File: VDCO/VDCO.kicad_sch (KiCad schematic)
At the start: 65 parts, among them J1 Conn_02x05_Counter_Clockwise, J2 ModeCV, J3 Parameter 1 CV, J4 Parameter 2 CV, J5 Gain CV, J6 Output, J7 V/OCT, SW1 Mode Switch On-Off-On, U1 TL072

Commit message: couple changes
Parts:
- C1, C10, C11, C12, C13, C14, C15, C2, C3, C4, C5, C6, C7, C8, C9: footprint Capacitor_THT:C_Disc_D5.0mm_W2.5mm_P5.00mm -> Capacitor_SMD:C_0805_2012Metric_Pad1.18x1.45mm_HandSolder
- D1, D10, D11, D12, D13, D3, D5, D6, D8, D9: footprint Diode_THT:D_DO-35_SOD27_P7.62mm_Horizontal -> Diode_SMD:D_0805_2012Metric_Pad1.15x1.40mm_HandSolder
- D2, D4, D7: footprint LED_THT:LED_D5.0mm -> LED_SMD:LED_0805_2012Metric_Pad1.15x1.40mm_HandSolder
- R1, R10, R11, R12, R13, R14, R15, R16, R17, R18, R19, R2, R20, R21, R22, R23, R3, R4, R5, R6, R7, R8, R9: footprint Resistor_THT:R_Axial_DIN0207_L6.3mm_D2.5mm_P10.16mm_Horizontal -> Resistor_SMD:R_0805_2012Metric_Pad1.20x1.40mm_HandSolder

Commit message: first complete routing of smd board
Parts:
- removed D1, D10, D11, D12, D13, D3, D5, D6, D8, D9: D_Schottky_Small, Diode_SMD:D_0805_2012Metric_Pad1.15x1.40mm_HandSolder, symbol Device:D_Schottky_Small
- removed SW1: Mode Switch On-Off-On, Button_Switch_THT:SW_CuK_JS202011CQN_DPDT_Straight, symbol Switch:SW_SPDT_MSM
- added D2, D4, D6, D7, D8: D_Zener_Small, Diode_SMD:D_0805_2012Metric_Pad1.15x1.40mm_HandSolder, symbol Device:D_Zener_Small
- added SW1: SW_SPDT, Button_Switch_THT:SW_PUSH_6mm_H5mm, symbol Switch:SW_SPST
- C13: renamed from C12; value 4.7u -> 10u
- D1: renamed from D2; footprint LED_SMD:LED_0805_2012Metric_Pad1.15x1.40mm_HandSolder -> LED_THT:LED_D5.0mm
- D3: renamed from D4; footprint LED_SMD:LED_0805_2012Metric_Pad1.15x1.40mm_HandSolder -> LED_THT:LED_D5.0mm
- D5: renamed from D7; footprint LED_SMD:LED_0805_2012Metric_Pad1.15x1.40mm_HandSolder -> LED_THT:LED_D5.0mm
- R14, R16: value 50K -> 47K
- R20: renamed from R18; value 220R -> 1K
- renumbered C13 to C12, J7 to J6, J6 to J7, R21 to R17, R22 to R18, R17 to R19, R19 to R21, R20 to R22
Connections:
- net GND: now also D2.2 (A), D4.2 (A), D6.2 (A), D7.2 (A), D8.2 (A), SW1.1 (A)
- net at A1.23 (A4), C9.1, R8.1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: now also D4.1 (K)
- net at A1.26 (A7), C12.1, R17.1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: now also D8.1 (K)
- net at A1.25 (A6), C11.1, R13.1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: now also D7.1 (K)
- net at A1.24 (A5), C10.1, R11.1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: now also D6.1 (K)
- net at A1.21 (A2), C8.1, R4.1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: now also D2.1 (K)
- net at A1.8 (D5): now also SW1.2 (B)
- no-connect marks 11 -> 12

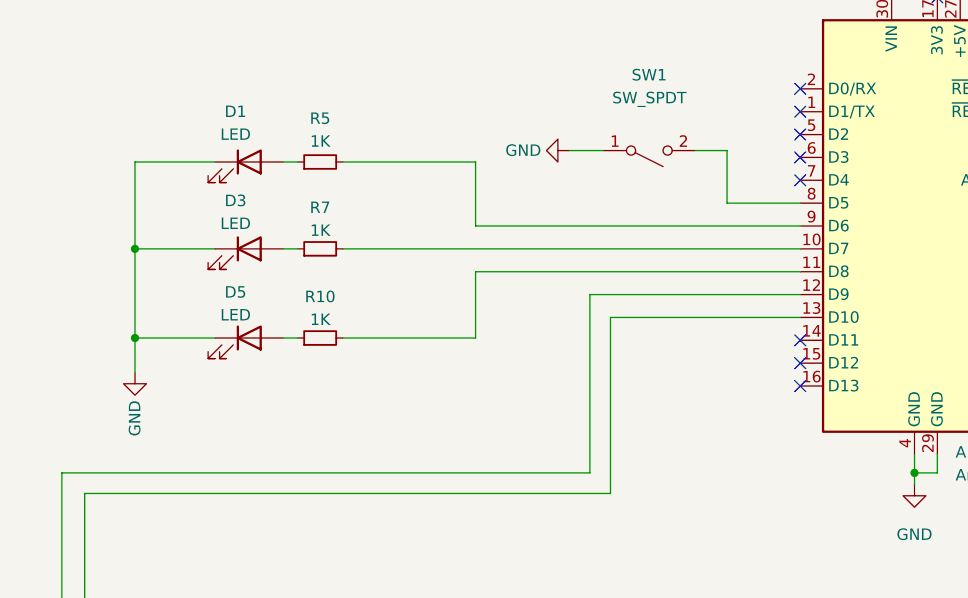
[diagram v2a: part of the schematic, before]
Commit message: remove one led, tighten up routing
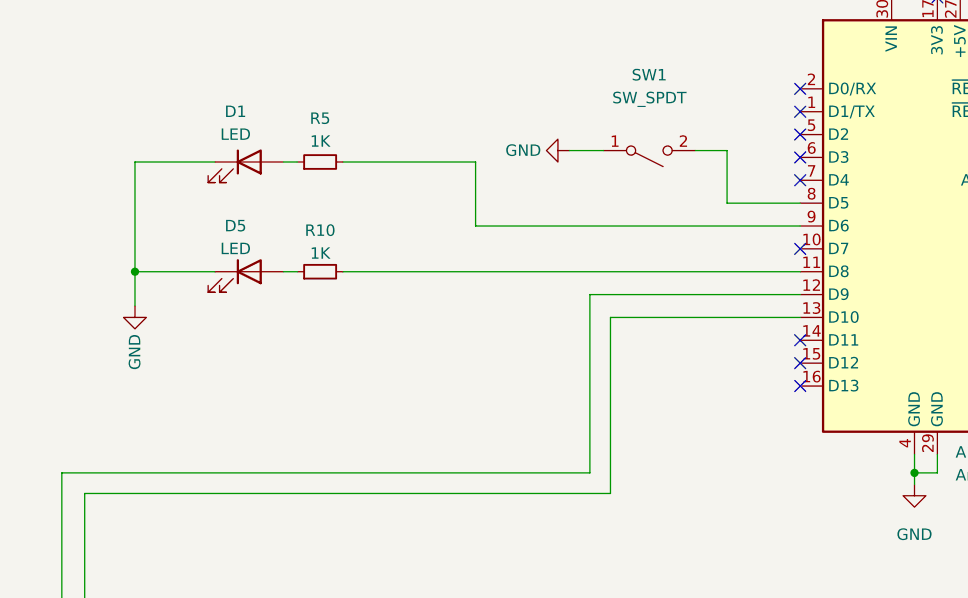
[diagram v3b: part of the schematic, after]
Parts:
- removed D3: LED, LED_THT:LED_D5.0mm, symbol Device:LED
- removed R7: 1K, Resistor_SMD:R_0805_2012Metric_Pad1.20x1.40mm_HandSolder, symbol Device:R_Small
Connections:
- no-connect marks 12 -> 13
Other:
- moved on the sheet: D5, R10
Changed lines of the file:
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@@
   (junction (at 233.426 118.11) (diameter 0) (color 0 0 0 0)
   )
+  (junction (at 29.718 90.424) (diameter 0) (color 0 0 0 0)
+  )
   (junction (at 244.602 136.906) (diameter 0) (color 0 0 0 0)
   )
@@
   (junction (at 226.822 41.91) (diameter 0) (color 0 0 0 0)
   )
-  (junction (at 29.718 97.79) (diameter 0) (color 0 0 0 0)
-  )
   (junction (at 232.918 131.826) (diameter 0) (color 0 0 0 0)
   )
@@
   )
   (junction (at 233.426 98.552) (diameter 0) (color 0 0 0 0)
-  )
-  (junction (at 29.718 87.884) (diameter 0) (color 0 0 0 0)
   )
   (no_connect (at 103.632 103.124))
   (no_connect (at 103.632 100.584))
   (no_connect (at 103.632 98.044))
+  (no_connect (at 103.632 87.884))
   (no_connect (at 103.632 70.104))
   (no_connect (at 129.032 70.104))
@@
     (stroke (width 0) (type default) (color 0 0 0 0))
   )
-  (wire (pts (xy 52.832 97.79) (xy 67.564 97.79))
+  (wire (pts (xy 52.832 90.424) (xy 103.632 90.424))
     (stroke (width 0) (type default) (color 0 0 0 0))
   )
@@
     (stroke (width 0) (type default) (color 0 0 0 0))
   )
-  (wire (pts (xy 52.832 87.884) (xy 103.632 87.884))
-    (stroke (width 0) (type default) (color 0 0 0 0))
-  )
   (wire (pts (xy 89.408 53.848) (xy 89.408 51.308))
     (stroke (width 0) (type default) (color 0 0 0 0))
@@
     (stroke (width 0) (type default) (color 0 0 0 0))
   )
-  (wire (pts (xy 29.718 97.79) (xy 38.608 97.79))
-    (stroke (width 0) (type default) (color 0 0 0 0))
-  )
-  (wire (pts (xy 29.718 87.884) (xy 38.608 87.884))
+  (wire (pts (xy 29.718 90.424) (xy 38.608 90.424))
     (stroke (width 0) (type default) (color 0 0 0 0))
   )
@@
     (stroke (width 0) (type default) (color 0 0 0 0))
   )
+  (wire (pts (xy 29.718 90.424) (xy 29.718 94.234))
+    (stroke (width 0) (type default) (color 0 0 0 0))
+  )
   (wire (pts (xy 91.694 43.688) (xy 91.694 46.228))
     (stroke (width 0) (type default) (color 0 0 0 0))
@@
     (stroke (width 0) (type default) (color 0 0 0 0))
   )
-  (wire (pts (xy 67.564 97.79) (xy 67.564 90.424))
-    (stroke (width 0) (type default) (color 0 0 0 0))
-  )
   (wire (pts (xy 226.314 75.692) (xy 233.934 75.692))
     (stroke (width 0) (type default) (color 0 0 0 0))
@@
     (stroke (width 0) (type default) (color 0 0 0 0))
   )
-  (wire (pts (xy 29.718 78.232) (xy 29.718 87.884))
-    (stroke (width 0) (type default) (color 0 0 0 0))
-  )
   (wire (pts (xy 219.456 80.772) (xy 219.71 80.772))
     (stroke (width 0) (type default) (color 0 0 0 0))
@@
     (stroke (width 0) (type default) (color 0 0 0 0))
   )
-  (wire (pts (xy 67.564 90.424) (xy 103.632 90.424))
-    (stroke (width 0) (type default) (color 0 0 0 0))
-  )
   (wire (pts (xy 82.55 95.504) (xy 82.55 115.062))
     (stroke (width 0) (type default) (color 0 0 0 0))
@@
     (stroke (width 0) (type default) (color 0 0 0 0))
   )
-  (wire (pts (xy 46.228 97.79) (xy 47.752 97.79))
+  (wire (pts (xy 46.228 90.424) (xy 47.752 90.424))
     (stroke (width 0) (type default) (color 0 0 0 0))
   )
@@
     (stroke (width 0) (type default) (color 0 0 0 0))
   )
-  (wire (pts (xy 29.718 87.884) (xy 29.718 97.79))
+  (wire (pts (xy 29.718 78.232) (xy 29.718 90.424))
     (stroke (width 0) (type default) (color 0 0 0 0))
   )
@@
   )
   (wire (pts (xy 76.708 38.608) (xy 76.708 41.148))
-    (stroke (width 0) (type default) (color 0 0 0 0))
-  )
-  (wire (pts (xy 46.228 87.884) (xy 47.752 87.884))
-    (stroke (width 0) (type default) (color 0 0 0 0))
-  )
-  (wire (pts (xy 29.718 97.79) (xy 29.718 101.6))
     (stroke (width 0) (type default) (color 0 0 0 0))
   )
@@
     (pin "2")
     (pin "3")
-  )
-  (symbol (lib_id "Device:LED") (at 42.418 87.884 0) (unit 1)
-    (in_bom yes) (on_board yes)
-    (property "Reference" "D3" (id 0) (at 40.894 82.55 0))
-    (property "Value" "LED" (id 1) (at 40.894 85.09 0))
-    (property "Footprint" "LED_THT:LED_D5.0mm" (id 2) (at 42.418 87.884 0)
-      (effects (font (size 1.27 1.27)) hide)
-    )
-    (property "Datasheet" "~" (id 3) (at 42.418 87.884 0)
-      (effects (font (size 1.27 1.27)) hide)
-    )
-    (pin "1")
-    (pin "2")
   )
   (symbol (lib_id "Device:R_Small") (at 244.602 134.366 180) (unit 1)
@@
     (pin "T")
   )
-  (symbol (lib_id "Device:LED") (at 42.418 97.79 0) (unit 1)
-    (in_bom yes) (on_board yes)
-    (property "Reference" "D5" (id 0) (at 40.894 92.71 0))
-    (property "Value" "LED" (id 1) (at 40.894 95.25 0))
-    (property "Footprint" "LED_THT:LED_D5.0mm" (id 2) (at 42.418 97.79 0)
-      (effects (font (size 1.27 1.27)) hide)
-    )
-    (property "Datasheet" "~" (id 3) (at 42.418 97.79 0)
+  (symbol (lib_id "Device:LED") (at 42.418 90.424 0) (unit 1)
+    (in_bom yes) (on_board yes)
+    (property "Reference" "D5" (id 0) (at 40.894 85.344 0))
+    (property "Value" "LED" (id 1) (at 40.894 87.884 0))
+    (property "Footprint" "LED_THT:LED_D5.0mm" (id 2) (at 42.418 90.424 0)
+      (effects (font (size 1.27 1.27)) hide)
+    )
+    (property "Datasheet" "~" (id 3) (at 42.418 90.424 0)
       (effects (font (size 1.27 1.27)) hide)
     )
@@
     )
     (pin "1")
-  )
-  (symbol (lib_id "Device:R_Small") (at 50.292 87.884 90) (unit 1)
-    (in_bom yes) (on_board yes)
-    (property "Reference" "R7" (id 0) (at 50.292 83.312 90))
-    (property "Value" "1K" (id 1) (at 50.292 85.852 90))
-    (property "Footprint" "Resistor_SMD:R_0805_2012Metric_Pad1.20x1.40mm_HandSolder" (id 2) (at 50.292 87.884 0)
-      (effects (font (size 1.27 1.27)) hide)
-    )
-    (property "Datasheet" "~" (id 3) (at 50.292 87.884 0)
-      (effects (font (size 1.27 1.27)) hide)
-    )
-    (pin "1")
-    (pin "2")
   )
   (symbol (lib_id "Device:C_Small") (at 220.218 48.514 0) (unit 1)
@@
     (pin "2")
   )
-  (symbol (lib_id "power:GND") (at 29.718 101.6 0) (unit 1)
-    (in_bom yes) (on_board yes)
-    (property "Reference" "#PWR016" (id 0) (at 29.718 107.95 0)
-      (effects (font (size 1.27 1.27)) hide)
-    )
-    (property "Value" "GND" (id 1) (at 29.718 108.712 90)
-      (effects (font (size 1.27 1.27)) (justify left))
-    )
-    (property "Footprint" "" (id 2) (at 29.718 101.6 0)
-      (effects (font (size 1.27 1.27)) hide)
-    )
-    (property "Datasheet" "" (id 3) (at 29.718 101.6 0)
-      (effects (font (size 1.27 1.27)) hide)
-    )
-    (pin "1")
-  )
-  (symbol (lib_id "Device:R_Small") (at 50.292 97.79 90) (unit 1)
-    (in_bom yes) (on_board yes)
-    (property "Reference" "R10" (id 0) (at 50.292 93.218 90))
-    (property "Value" "1K" (id 1) (at 50.292 95.758 90))
-    (property "Footprint" "Resistor_SMD:R_0805_2012Metric_Pad1.20x1.40mm_HandSolder" (id 2) (at 50.292 97.79 0)
-      (effects (font (size 1.27 1.27)) hide)
-    )
-    (property "Datasheet" "~" (id 3) (at 50.292 97.79 0)
+  (symbol (lib_id "power:GND") (at 29.718 94.234 0) (unit 1)
+    (in_bom yes) (on_board yes)
+    (property "Reference" "#PWR016" (id 0) (at 29.718 100.584 0)
+      (effects (font (size 1.27 1.27)) hide)
+    )
+    (property "Value" "GND" (id 1) (at 29.718 101.346 90)
+      (effects (font (size 1.27 1.27)) (justify left))
+    )
+    (property "Footprint" "" (id 2) (at 29.718 94.234 0)
+      (effects (font (size 1.27 1.27)) hide)
+    )
+    (property "Datasheet" "" (id 3) (at 29.718 94.234 0)
+      (effects (font (size 1.27 1.27)) hide)
+    )
+    (pin "1")
+  )
+  (symbol (lib_id "Device:R_Small") (at 50.292 90.424 90) (unit 1)
+    (in_bom yes) (on_board yes)
+    (property "Reference" "R10" (id 0) (at 50.292 85.852 90))
+    (property "Value" "1K" (id 1) (at 50.292 88.392 90))
+    (property "Footprint" "Resistor_SMD:R_0805_2012Metric_Pad1.20x1.40mm_HandSolder" (id 2) (at 50.292 90.424 0)
+      (effects (font (size 1.27 1.27)) hide)
+    )
+    (property "Datasheet" "~" (id 3) (at 50.292 90.424 0)
       (effects (font (size 1.27 1.27)) hide)
     )
@@
       (reference "D2") (unit 1) (value "D_Zener_Small") (footprint "Diode_SMD:D_0805_2012Metric_Pad1.15x1.40mm_HandSolder")
     )
-    (path "/19de9007-8b20-4d5d-b314-6750d865ace7"
-      (reference "D3") (unit 1) (value "LED") (footprint "LED_THT:LED_D5.0mm")
-    )
     (path "/5f8649b2-394d-4d7a-a214-6c2ff9070cba"
       (reference "D4") (unit 1) (value "D_Zener_Small") (footprint "Diode_SMD:D_0805_2012Metric_Pad1.15x1.40mm_HandSolder")
@@
       (reference "R6") (unit 1) (value "100K") (footprint "Resistor_SMD:R_0805_2012Metric_Pad1.20x1.40mm_HandSolder")
     )
-    (path "/6584334d-5052-47ca-a6ee-d4fbf5e71132"
-      (reference "R7") (unit 1) (value "1K") (footprint "Resistor_SMD:R_0805_2012Metric_Pad1.20x1.40mm_HandSolder")
-    )
     (path "/01591145-90c4-4e8f-94f8-54633925b334"
